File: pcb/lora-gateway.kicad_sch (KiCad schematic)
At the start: 10 parts, among them J1 USB_B_Micro, J2 Conn_01x06, J3 Conn_01x06, J4 Conn_Coaxial, U1 RFM95W-868S2, U2 ATmega2560-16A, U3 LM1117-3.3

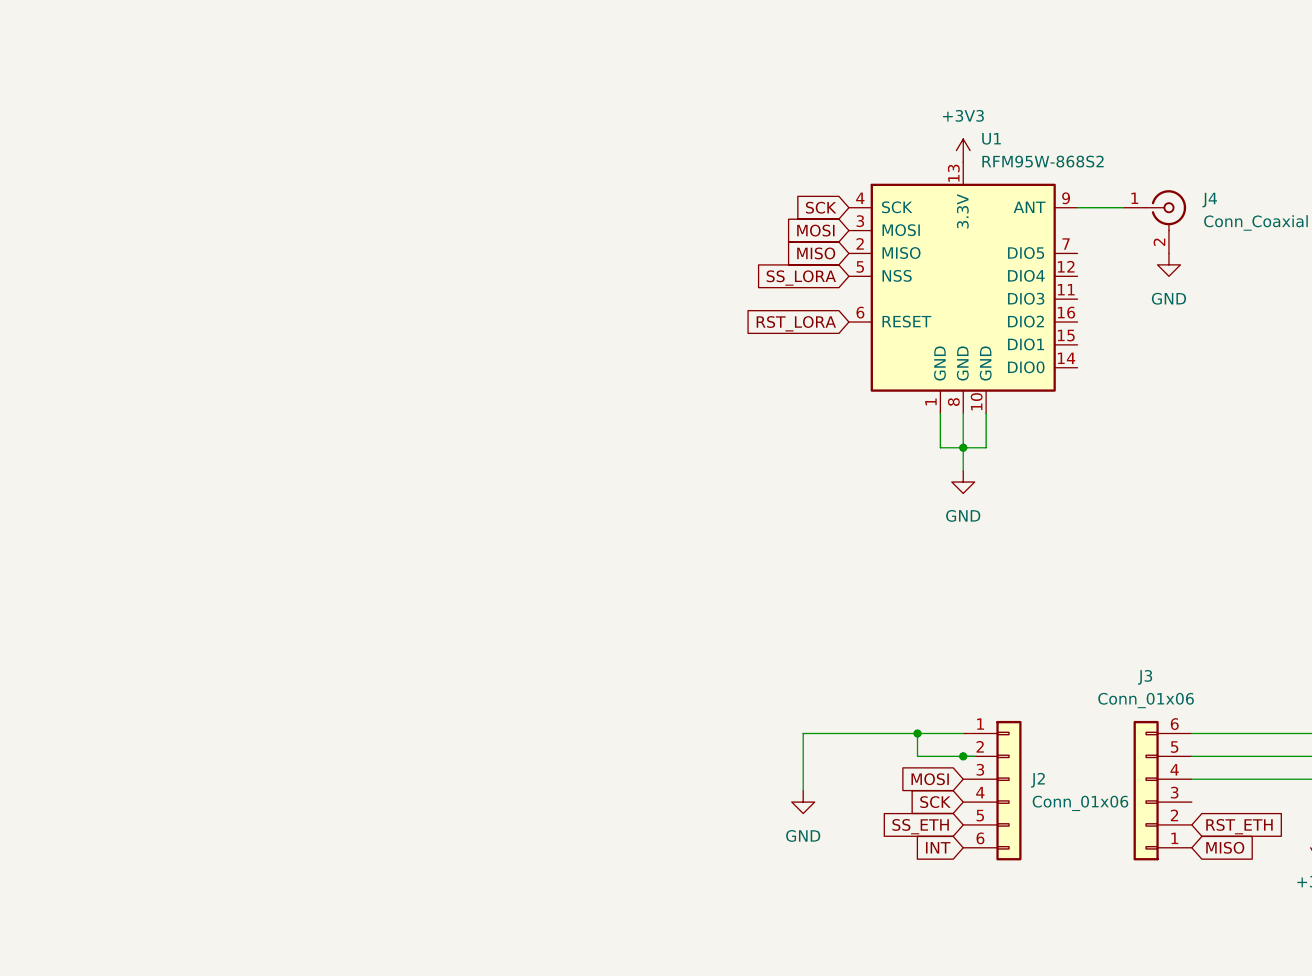
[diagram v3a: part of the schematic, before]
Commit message: add isp + jtag connector
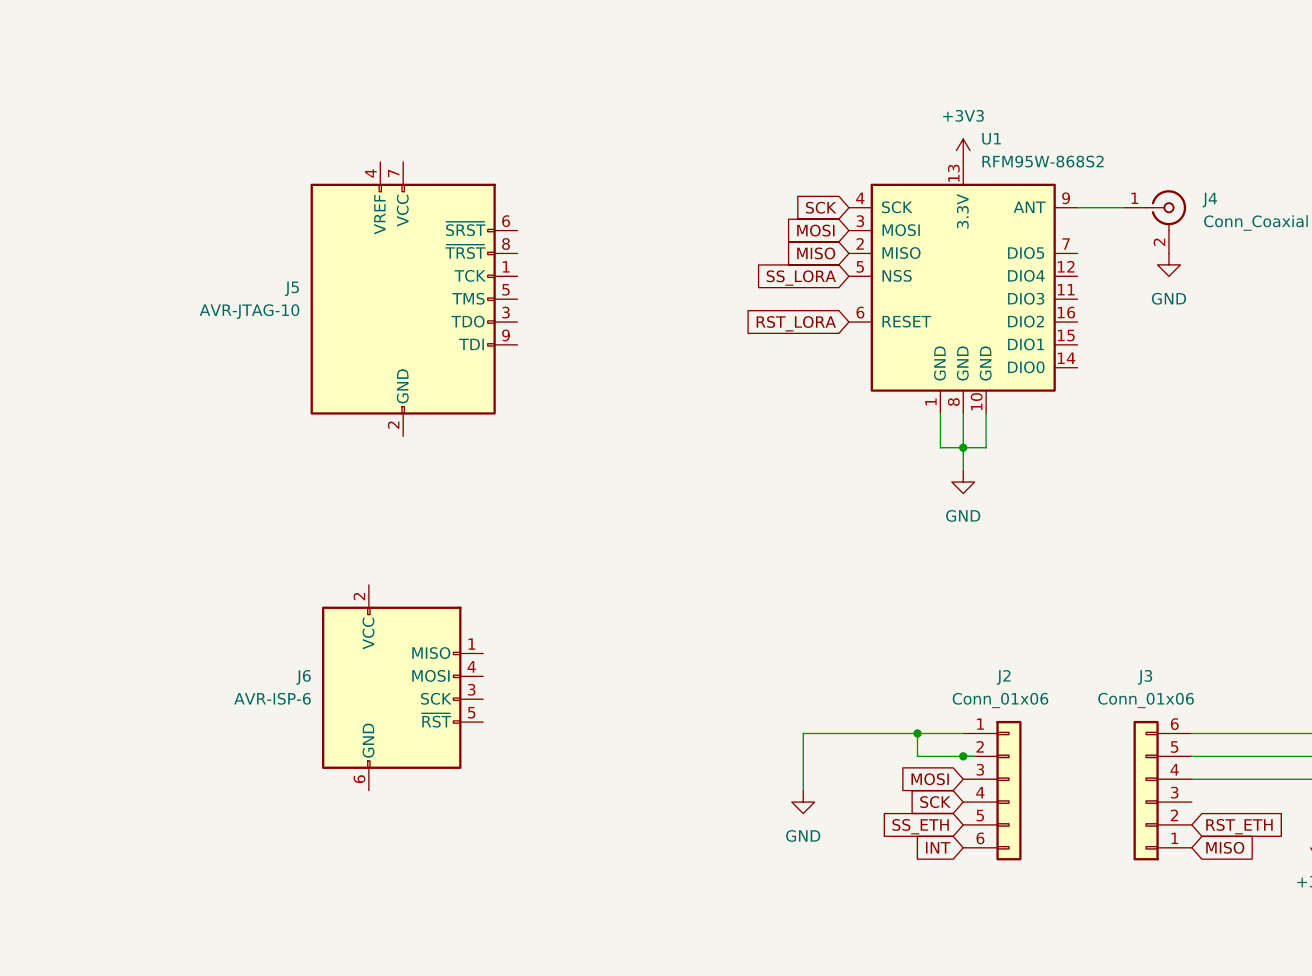
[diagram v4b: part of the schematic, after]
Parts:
- added J5: AVR-JTAG-10, symbol Connector:AVR-JTAG-10
- added J6: AVR-ISP-6, symbol Connector:AVR-ISP-6
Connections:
- new net: J5.10 (GND), J5.2 (GND)
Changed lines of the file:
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@@
   )
   (symbol (lib_id "Connector_Generic:Conn_01x06") (at 224.79 99.06 0) (unit 1)
-    (in_bom yes) (on_board yes) (dnp no) (fields_autoplaced)
-    (property "Reference" "J2" (at 227.33 99.06 0)
-      (effects (font (size 1.27 1.27)) (justify left))
-    )
-    (property "Value" "Conn_01x06" (at 227.33 101.6 0)
+    (in_bom yes) (on_board yes) (dnp no)
+    (property "Reference" "J2" (at 223.52 87.63 0)
+      (effects (font (size 1.27 1.27)) (justify left))
+    )
+    (property "Value" "Conn_01x06" (at 218.44 90.17 0)
       (effects (font (size 1.27 1.27)) (justify left))
     )
@@
         (path "/5fd0eb65-7f10-4bbb-b642-b528dcb1ea0e"
           (reference "#PWR06") (unit 1)
+        )
+      )
+    )
+  )
+  (symbol (lib_id "Connector:AVR-JTAG-10") (at 157.48 45.72 0) (unit 1)
+    (in_bom yes) (on_board yes) (dnp no) (fields_autoplaced)
+    (property "Reference" "J5" (at 146.05 44.45 0)
+      (effects (font (size 1.27 1.27)) (justify right))
+    )
+    (property "Value" "AVR-JTAG-10" (at 146.05 46.99 0)
+      (effects (font (size 1.27 1.27)) (justify right))
+    )
+    (property "Footprint" "" (at 153.67 41.91 90)
+      (effects (font (size 1.27 1.27)) hide)
+    )
+    (property "Datasheet" " ~" (at 125.095 59.69 0)
+      (effects (font (size 1.27 1.27)) hide)
+    )
+    (pin "1")
+    (pin "10")
+    (pin "2")
+    (pin "3")
+    (pin "4")
+    (pin "5")
+    (pin "6")
+    (pin "7")
+    (pin "8")
+    (pin "9")
+    (instances
+      (project "lora-gateway"
+        (path "/5fd0eb65-7f10-4bbb-b642-b528dcb1ea0e"
+          (reference "J5") (unit 1)
         )
       )
@@
         )
       )
+    )
+  )
+  (symbol (lib_id "Connector:AVR-ISP-6") (at 156.21 90.17 0) (unit 1)
+    (in_bom yes) (on_board yes) (dnp no) (fields_autoplaced)
+    (property "Reference" "J6" (at 147.32 87.63 0)
+      (effects (font (size 1.27 1.27)) (justify right))
+    )
+    (property "Value" "AVR-ISP-6" (at 147.32 90.17 0)
+      (effects (font (size 1.27 1.27)) (justify right))
+    )
+    (property "Footprint" "" (at 149.86 88.9 90)
+      (effects (font (size 1.27 1.27)) hide)
+    )
+    (property "Datasheet" " ~" (at 123.825 104.14 0)
+      (effects (font (size 1.27 1.27)) hide)
+    )
+    (pin "1")
+    (pin "2")
+    (pin "3")
+    (pin "4")
+    (pin "5")
+    (pin "6")
+    (instances
+      (project "lora-gateway"
+        (path "/5fd0eb65-7f10-4bbb-b642-b528dcb1ea0e"
+          (reference "J6") (unit 1)
+        )
+      )

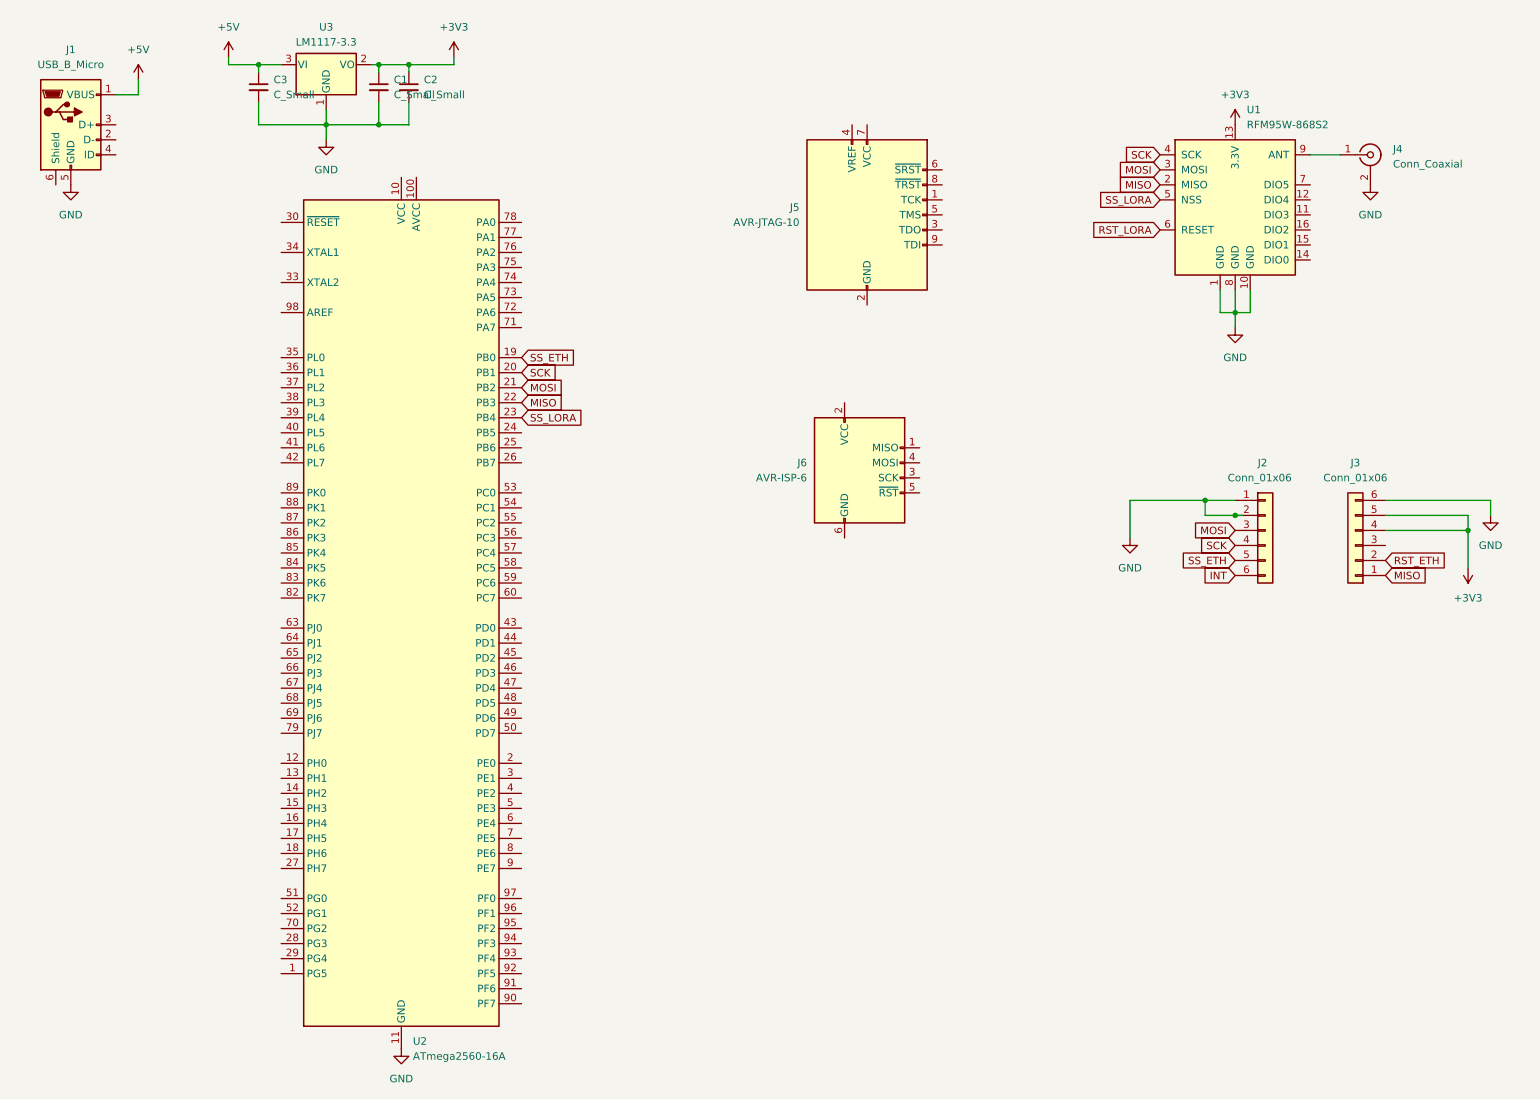
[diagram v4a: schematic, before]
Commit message: add isp + jtag connector
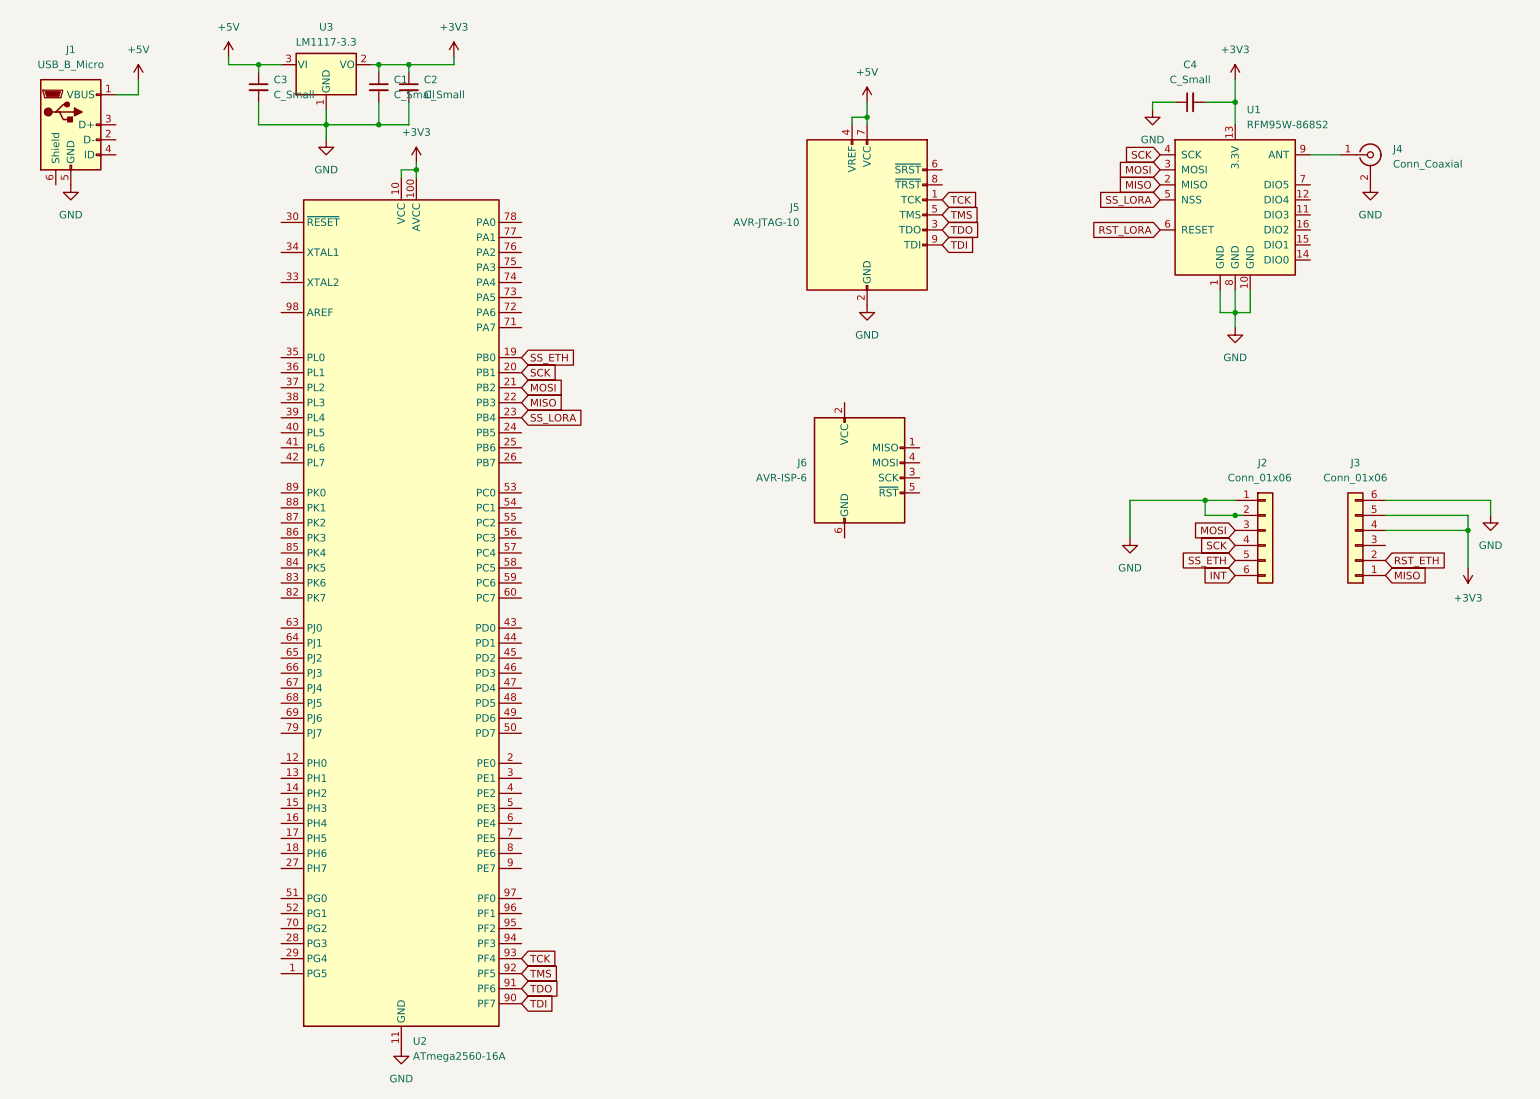
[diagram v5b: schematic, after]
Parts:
- added C4: C_Small, Capacitor_SMD:C_0603_1608Metric, symbol Device:C_Small
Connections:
- net +3V3: now also U2.10 (VCC), U2.100 (AVCC), U2.31 (VCC), U2.61 (VCC), U2.80 (VCC), C4.2
- net +5V: now also J5.4 (VREF), J5.7 (VCC)
- net GND: now also J5.10 (GND), J5.2 (GND), C4.1
- net TDI: now reaches U2.90 (PF7)
- net TDI: now also J5.9 (TDI)
- net TDO: now reaches U2.91 (PF6)
- net TDO: now also J5.3 (TDO)
- net TMS: now reaches U2.92 (PF5)
- net TMS: now also J5.5 (TMS)
- net TCK: now reaches U2.93 (PF4)
- net TCK: now also J5.1 (TCK)

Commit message: pcb wiring
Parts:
- added C5, C6: C_Small, Capacitor_SMD:C_0603_1608Metric, symbol Device:C_Small
- added R1: R_Small, Resistor_SMD:R_0603_1608Metric, symbol Device:R_Small
- added SW1: SW_Push, Button_Switch_SMD:SW_SPST_CK_RS282G05A3, symbol Switch:SW_Push
- added Y1: Crystal, Crystal:Crystal_SMD_5032-2Pin_5.0x3.2mm, symbol Device:Crystal
- J5: footprint (none) -> Connector_PinHeader_2.54mm:PinHeader_2x05_P2.54mm_Vertical
- J6: footprint (none) -> Connector_PinHeader_2.54mm:PinHeader_2x03_P2.54mm_Vertical
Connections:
- net +3V3: now also R1.1
- net +5V: now also J6.2 (VCC)
- net GND: now also J6.6 (GND), C5.2, C6.2, SW1.1
- net MISO: now also J6.1 (MISO)
- net MOSI: now also J6.4 (MOSI)
- net SCK: now also J6.3 (SCK)
- net RST: now reaches U2.30 (~{RESET})
- net RST: now also J5.6 (~{SRST}), J6.5 (~{RST}), R1.2, SW1.2
- net at U2.33 (XTAL2): now also C6.1, Y1.2
- net at U2.34 (XTAL1): now also C5.1, Y1.1
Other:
- moved on the sheet: C1, C2, C3, U2, U3

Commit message: up schematic
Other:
- note added: "ISP CONNECTOR"
- note added: "JTAG CONNECTOR"
- note added: "LORA RFM95"
- note added: "MICRO-USB"
- note added: "Regulator"
- note added: "USR ES1"
- note added: "m2560"
- moved on the sheet: C1, C2, C3, J1, J6, U3
